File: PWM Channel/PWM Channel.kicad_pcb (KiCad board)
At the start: 4 copper layers, 10 parts, among them J101 Conn_01x05_Male, U201 NE555P

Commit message: Working on comparator
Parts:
- added C301: 0.1uF, Capacitor_THT:C_Disc_D4.3mm_W1.9mm_P5.00mm, F.Cu at (14.0, 21.6)
- added C302: 0.1uF, Capacitor_THT:C_Disc_D4.3mm_W1.9mm_P5.00mm, F.Cu at (40.6, -8.89)
- added C303: 0.1uF, Capacitor_THT:C_Disc_D4.3mm_W1.9mm_P5.00mm, F.Cu at (14.0, 52.1)
- added C304: 0.1uF, Capacitor_THT:C_Disc_D4.3mm_W1.9mm_P5.00mm, F.Cu at (67.3, 16.5)
- added C305: 0.1uF, Capacitor_THT:C_Disc_D4.3mm_W1.9mm_P5.00mm, F.Cu at (83.8, 16.5)
- added C306: 0.1uF, Capacitor_THT:C_Disc_D4.3mm_W1.9mm_P5.00mm, F.Cu at (97.8, 16.5)
- added U301: 74HCT595, Package_DIP:DIP-16_W7.62mm_Socket, F.Cu at (12.7, 25.4)
- added U302: 4040, Package_DIP:DIP-16_W7.62mm_Socket, F.Cu at (39.4, -5.08)
- added U303: 74HCT595, Package_DIP:DIP-16_W7.62mm_Socket, F.Cu at (12.7, 55.9)
- added U304: 7485, Package_DIP:DIP-16_W7.62mm_Socket, F.Cu at (66.0, 20.3)
- added U305: 7485, Package_DIP:DIP-16_W7.62mm_Socket, F.Cu at (82.5, 20.3)
- added U306: 7485, Package_DIP:DIP-16_W7.62mm_Socket, F.Cu at (96.5, 20.3)
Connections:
- net /Driver Clock/PWMCLK renamed /PWM/DRIVER

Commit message: Starting rough routing
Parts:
- removed C301, C303: 0.1uF, Capacitor_THT:C_Disc_D4.3mm_W1.9mm_P5.00mm
- removed U301, U303: 74HCT595, Package_DIP:DIP-16_W7.62mm_Socket
- added C401: 0.1uF, Capacitor_THT:C_Disc_D4.3mm_W1.9mm_P5.00mm, F.Cu at (26.7, 17.8)
- added C402: 0.1uF, Capacitor_THT:C_Disc_D4.3mm_W1.9mm_P5.00mm, F.Cu at (26.7, 47.0)
- added D101: LED, LED_THT:LED_D5.0mm, F.Cu at (83.8, 66.0)
- added R101: R, Resistor_THT:R_Axial_DIN0207_L6.3mm_D2.5mm_P7.62mm_Horizontal, F.Cu at (83.8, 58.4)
- added U401: 74HCT595, Package_DIP:DIP-16_W7.62mm_Socket, F.Cu at (25.4, 22.9)
- added U402: 74HCT595, Package_DIP:DIP-16_W7.62mm_Socket, F.Cu at (25.4, 50.8)
- moved J101 58.8 mm to (6.35, 58.4)
- moved C201 43.2 mm to (69.2, 6.35), turned to 0 degrees
- moved C202 40.2 mm to (71.1, -11.4)
- moved RV201 40.2 mm to (58.4, -5.08)
- moved C203 40.2 mm to (77.5, 3.81)
- moved R201 40.2 mm to (63.5, -11.4)
- moved R202 40.2 mm to (63.5, -1.27)
- moved R203 40.2 mm to (82.5, -11.4)
- moved U201 40.2 mm to (69.8, -7.62)
- moved C101 27.7 mm to (6.35, 31.8)
- moved U305 18.0 mm to (64.8, 22.9)
- moved C305 18.0 mm to (66.0, 19.1)
- moved C304 16.7 mm to (50.8, 19.1)
- moved C306 16.7 mm to (81.3, 19.1)
- moved U304 16.7 mm to (49.5, 22.9)
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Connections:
- net Net-(U302-Pad1) renamed /PWM/A11
- net Net-(U302-Pad12) renamed /PWM/A08
- net Net-(U302-Pad13) renamed /PWM/A07
- net Net-(U302-Pad14) renamed /PWM/A09
- net Net-(U302-Pad15) renamed /PWM/A10
- net Net-(U302-Pad2) renamed /PWM/A05
- net Net-(U302-Pad3) renamed /PWM/A04
- net Net-(U302-Pad4) renamed /PWM/A06
- net Net-(U302-Pad5) renamed /PWM/A03
- net Net-(U302-Pad6) renamed /PWM/A02
- net Net-(U302-Pad7) renamed /PWM/A01
- net Net-(U302-Pad9) renamed /PWM/A00
- J101 pad 2: Net-(J101-Pad2) -> /SPI Input/CLK
- J101 pad 3: Net-(J101-Pad3) -> /SPI Input/COPI
- J101 pad 4: Net-(J101-Pad4) -> /SPI Input/~SELECT
- U304 pad 1: Net-(U303-Pad4) -> /PWM/B03
- U304 pad 11: Net-(U303-Pad6) -> /PWM/B01
- U304 pad 14: Net-(U303-Pad5) -> /PWM/B02
- U304 pad 9: Net-(U303-Pad7) -> /PWM/B00
- U305 pad 1: Net-(U303-Pad15) -> /PWM/B07
- U305 pad 11: Net-(U303-Pad2) -> /PWM/B05
- U305 pad 14: Net-(U303-Pad1) -> /PWM/B06
- U305 pad 9: Net-(U303-Pad3) -> /PWM/B04
- U306 pad 1: Net-(U301-Pad7) -> /PWM/B11
- U306 pad 11: Net-(U301-Pad5) -> /PWM/B09
- U306 pad 14: Net-(U301-Pad6) -> /PWM/B10
- U306 pad 9: Net-(U301-Pad4) -> /PWM/B08
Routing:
- net Net-(U305-Pad5): track 0.00 -> 45.5 mm
- net Net-(U304-Pad5): track 0.00 -> 45.5 mm
- net Net-(U305-Pad6): track 0.00 -> 43.0 mm
- net Net-(U304-Pad6): track 0.00 -> 43.0 mm
- net Net-(U304-Pad7): track 0.00 -> 40.4 mm
- net Net-(U305-Pad7): track 0.00 -> 40.4 mm
- net /PWM/B03: track 0.00 -> 28.2 mm
- net /PWM/A08: track 0.00 -> 27.6 mm
- net /PWM/B07: track 0.00 -> 27.6 mm
- net /PWM/B11: track 0.00 -> 26.9 mm
- net /PWM/A04: track 0.00 -> 25.7 mm
- net /PWM/A00: track 0.00 -> 25.0 mm
- net /PWM/A09: track 0.00 -> 21.2 mm
- net /PWM/A05: track 0.00 -> 19.9 mm
- net /PWM/B02: track 0.00 -> 19.9 mm
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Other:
- copper layers 4 -> 2

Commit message: More routing.... not very happy
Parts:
- moved C402 1.27 mm to (26.7, 45.7)
- moved C302 1.27 mm to (26.7, -12.7)
- moved C304 1.27 mm to (50.8, 17.8)
- moved C305 1.27 mm to (66.0, 17.8)
- moved C306 1.27 mm to (81.3, 17.8)
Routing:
- net /PWM/A10: track 17.4 -> 115.9 mm
- net /PWM/A11: track 11.1 -> 103.9 mm
- net /PWM/B11: track 26.9 -> 111.9 mm, vias 0 -> 1
- net /PWM/B10: track 18.7 -> 103.0 mm, vias 0 -> 1
- net /SPI Input/CLK: track 0.00 -> 84.1 mm, vias 0 -> 1
- net /PWM/B09: track 10.1 -> 88.3 mm, vias 0 -> 1
- net /PWM/A09: track 21.2 -> 95.6 mm
- net /PWM/B08: track 4.71 -> 78.5 mm, vias 0 -> 1
- net /PWM/A05: track 19.9 -> 91.2 mm, vias 0 -> 1
- net /PWM/A08: track 27.6 -> 97.9 mm, vias 0 -> 1
- net /PWM/A04: track 25.7 -> 94.3 mm
- net /PWM/A06: track 16.8 -> 82.3 mm, vias 0 -> 2
- net /SPI Input/~SELECT: track 0.00 -> 65.5 mm, vias 0 -> 2
- net /SPI Input/COPI: track 0.00 -> 60.7 mm
- net /PWM/A07: track 11.1 -> 68.7 mm, vias 0 -> 1
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
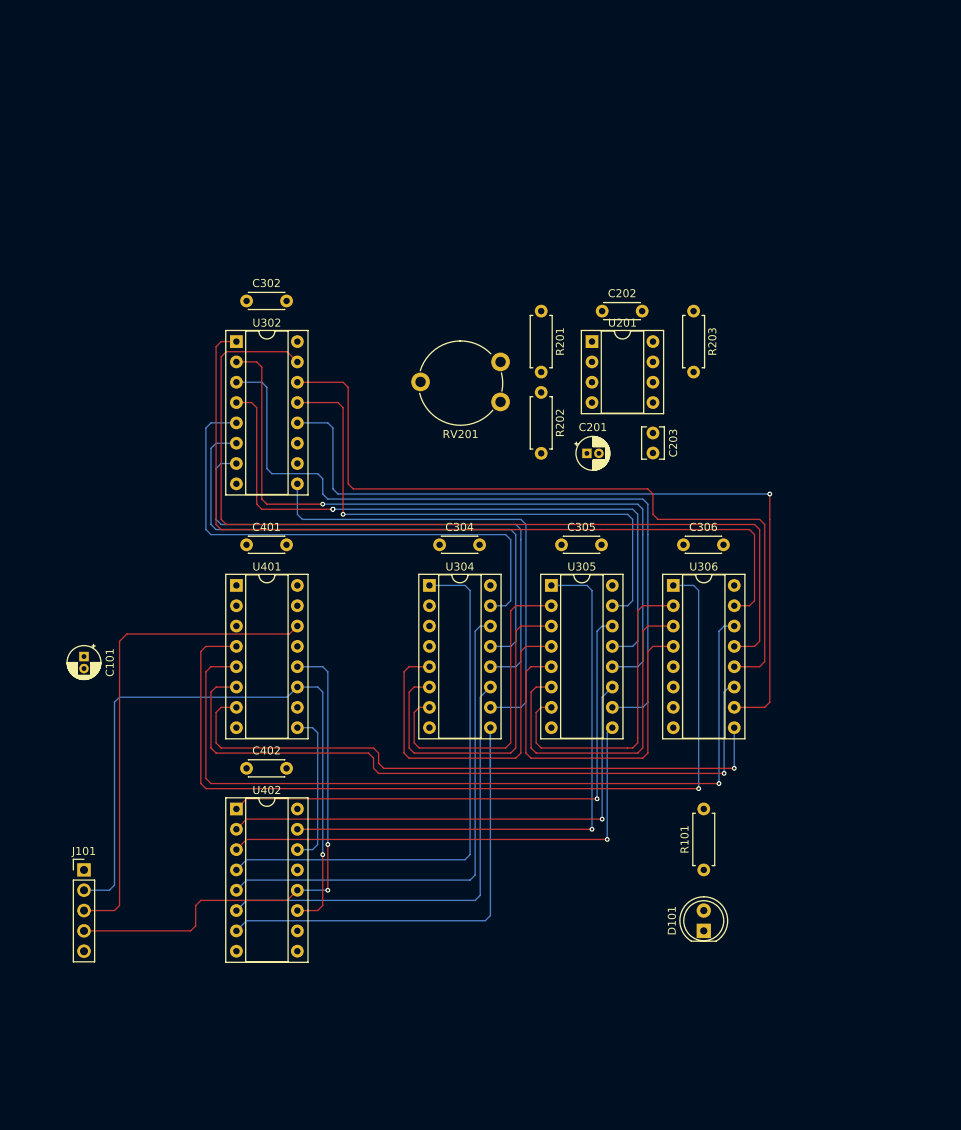
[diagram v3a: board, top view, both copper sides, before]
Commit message: Rerouting everything
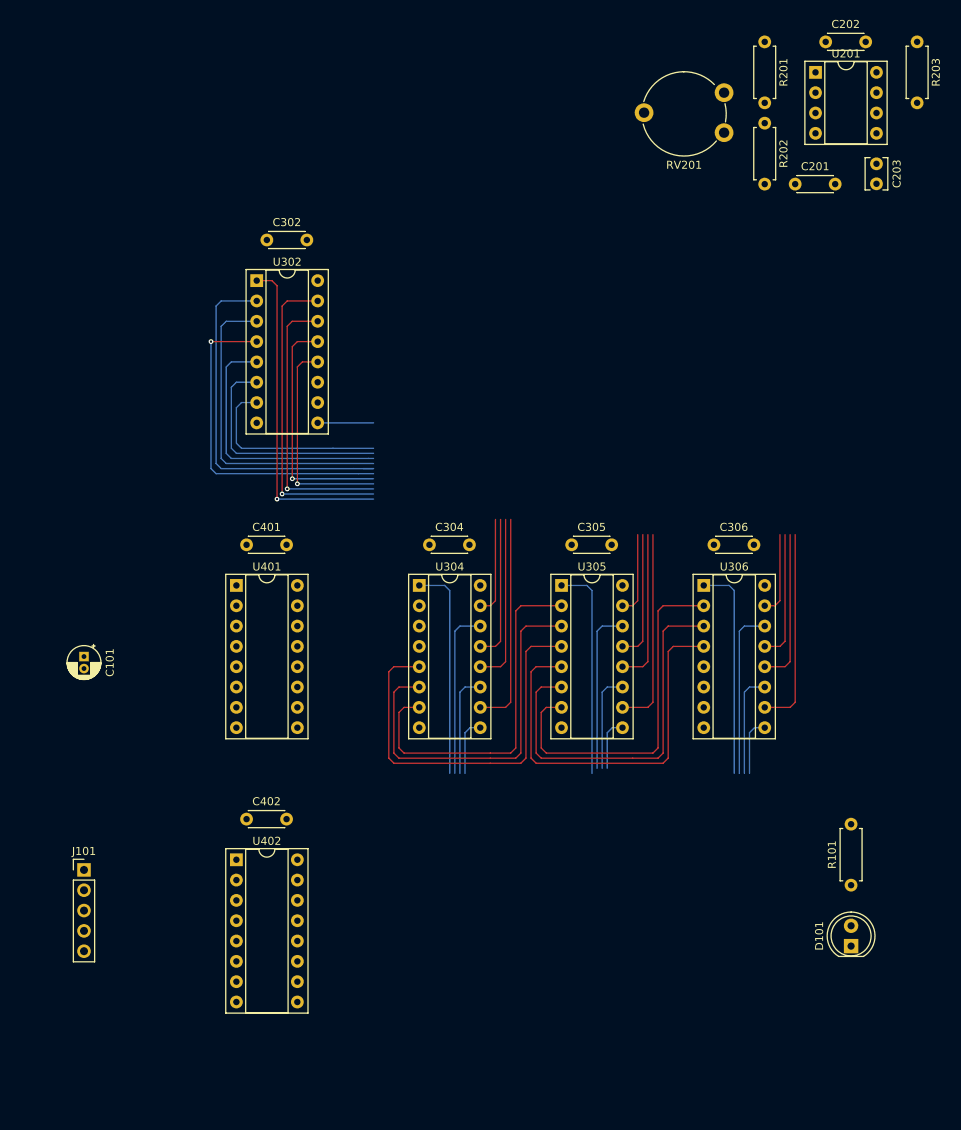
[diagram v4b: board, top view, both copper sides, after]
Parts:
- C201: value 1uF -> 0.1uF; footprint Capacitor_THT:CP_Radial_D4.0mm_P1.50mm -> Capacitor_THT:C_Disc_D4.3mm_W1.9mm_P5.00mm
- moved U201 43.7 mm to (97.8, -41.3)
- moved C202 43.7 mm to (99.1, -45.1)
- moved C203 43.7 mm to (105.4, -29.8)
- moved R201 43.7 mm to (91.4, -45.1)
- moved R203 43.7 mm to (110.5, -45.1)
- moved RV201 43.7 mm to (86.4, -38.7)
- moved R202 43.7 mm to (91.4, -34.9)
- moved C201 42.5 mm to (95.2, -27.3)
- moved D101 18.5 mm to (102.2, 67.9)
- moved R101 18.5 mm to (102.2, 60.3)
- moved U302 8.03 mm to (27.9, -15.2)
- moved C302 8.03 mm to (29.2, -20.3)
- moved C402 6.35 mm to (26.7, 52.1)
- moved U402 6.35 mm to (25.4, 57.1)
- moved C306 3.81 mm to (85.1, 17.8)
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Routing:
- net /PWM/B11: track 111.9 -> 26.9 mm, vias 1 -> 0
- net /SPI Input/CLK: track 84.1 -> 0.00 mm, vias 1 -> 0
- net /PWM/B10: track 103.0 -> 21.2 mm, vias 1 -> 0
- net /PWM/B09: track 88.3 -> 13.0 mm, vias 1 -> 0
- net /PWM/B08: track 78.5 -> 7.25 mm, vias 1 -> 0
- net /SPI Input/~SELECT: track 65.5 -> 0.00 mm, vias 2 -> 0
- net /SPI Input/COPI: track 60.7 -> 0.00 mm
- net /PWM/A10: track 115.9 -> 55.8 mm, vias 0 -> 1
- net /PWM/B04: track 61.1 -> 6.61 mm, vias 1 -> 0
- net /PWM/B00: track 61.7 -> 7.25 mm
- net /PWM/A11: track 103.9 -> 52.0 mm, vias 0 -> 1
- net /PWM/B05: track 63.3 -> 12.3 mm, vias 1 -> 0
- net /PWM/B06: track 68.7 -> 20.6 mm, vias 1 -> 0
- net /PWM/A08: track 97.9 -> 52.0 mm
- net /PWM/B07: track 72.0 -> 26.9 mm, vias 1 -> 0
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
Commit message: Preliminary routing
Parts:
- R201, R202: value 33 -> 4.7
- moved R203 76.4 mm to (43.2, -8.89)
- moved C201 36.4 mm to (69.8, -1.27)
- moved C202 36.4 mm to (73.7, -19.1)
- moved RV201 36.4 mm to (61.0, -12.7)
- moved U201 36.4 mm to (72.4, -15.2)
- moved C203 36.4 mm to (80.0, -3.81)
- moved R201 36.4 mm to (66.0, -19.1)
- moved R202 36.4 mm to (66.0, -8.89)
- moved D101 22.2 mm to (80.0, 67.3)
- moved R101 22.2 mm to (80.0, 59.7)
- moved C101 16.2 mm to (17.8, 20.3)
- moved J101 6.48 mm to (12.7, 59.7)
- moved C402 5.08 mm to (26.7, 47.0)
- moved U402 5.08 mm to (25.4, 52.1)
- moved U302 2.54 mm to (25.4, -15.2)
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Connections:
- J101 pad 2: /SPI Input/CLK -> /SPI Input/~SELECT
- J101 pad 4: /SPI Input/~SELECT -> /SPI Input/CLK
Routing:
- net /PWM/B11: track 26.9 -> 191.9 mm, vias 0 -> 1
- net /PWM/B10: track 21.2 -> 181.8 mm, vias 0 -> 1
- net /PWM/B09: track 13.0 -> 169.7 mm, vias 0 -> 1
- net /PWM/B08: track 7.25 -> 158.9 mm, vias 0 -> 1
- net /PWM/B07: track 26.9 -> 170.2 mm, vias 0 -> 1
- net /PWM/B06: track 20.6 -> 134.8 mm, vias 0 -> 1
- net /PWM/B05: track 12.3 -> 122.1 mm, vias 0 -> 1
- net /PWM/B04: track 6.61 -> 111.9 mm, vias 0 -> 1
- net /SPI Input/COPI: track 0.00 -> 93.8 mm
- net /PWM/B03: track 26.9 -> 106.8 mm, vias 0 -> 1
- net /PWM/B02: track 21.2 -> 96.7 mm, vias 0 -> 1
- net /PWM/B01: track 13.0 -> 84.0 mm, vias 0 -> 1
- net /PWM/B00: track 7.25 -> 73.8 mm, vias 0 -> 1
- net /PWM/A08: track 52.0 -> 113.6 mm, vias 1 -> 2
- net /PWM/A09: track 54.5 -> 114.8 mm, vias 1 -> 2
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- added copper zone on B.Cu, net +5V
- added copper zone on F.Cu, net GND
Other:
- board outline added: 94 x 111.8 mm
- board text added: "+5V"
- board text added: "CLK"
- board text added: "COPI"
- board text added: "GND"
- board text added: "PWM Channel"
- board text added: "RGE2021"
- board text added: "~SELECT"

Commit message: Add mounting holes
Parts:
- added H101: MountingHole, MountingHole:MountingHole_2.7mm_M2.5, F.Cu at (10.2, -22.9)
- added H102: MountingHole, MountingHole:MountingHole_2.7mm_M2.5, F.Cu at (94.0, -22.9)
- added H103: MountingHole, MountingHole:MountingHole_2.7mm_M2.5, F.Cu at (10.2, 78.7)
- added H104: MountingHole, MountingHole:MountingHole_2.7mm_M2.5, F.Cu at (94.0, 78.7)
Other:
- board text added: "Output"
